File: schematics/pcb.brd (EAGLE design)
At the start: 86.4 x 110.2 mm, 39 parts, among them IC1 7805TV, IC2 4050D, IC3 LP298XS, Q1 16Mhz, Q2 16Mhz, X1 MICROSD

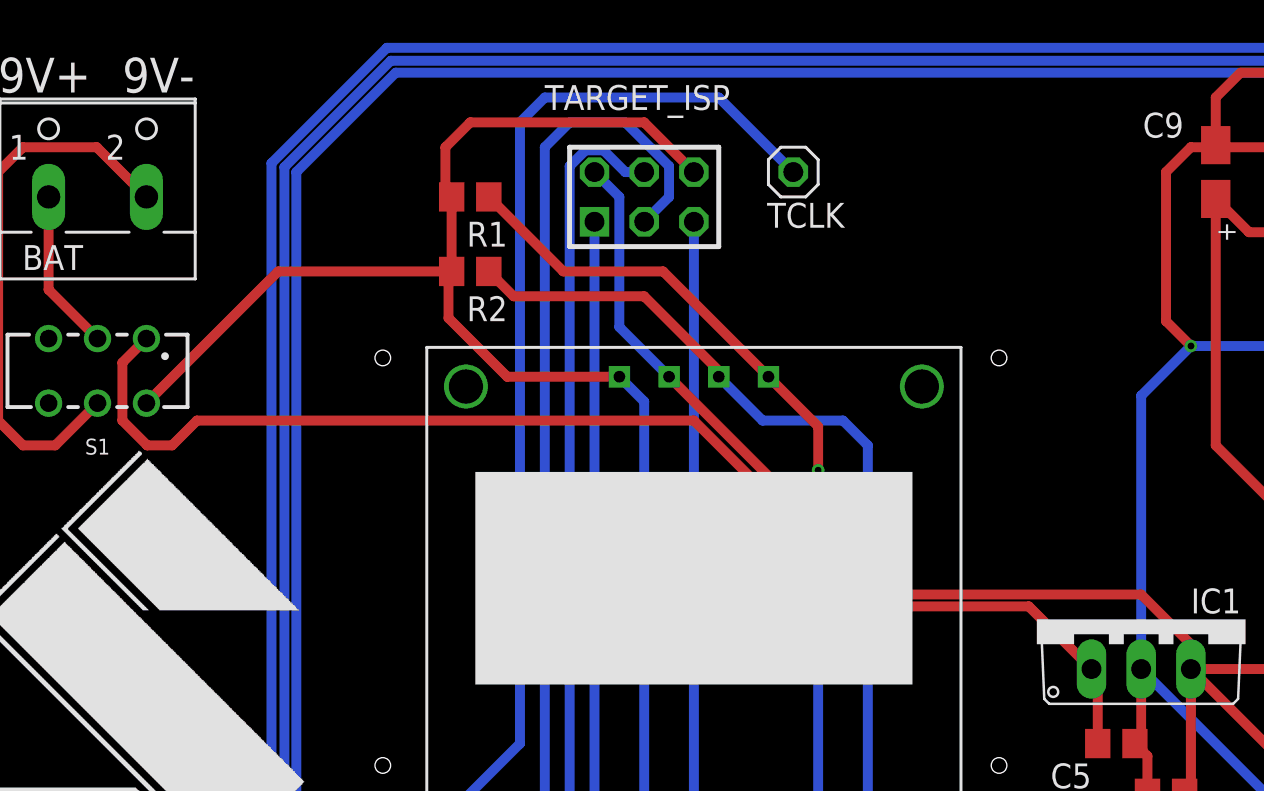
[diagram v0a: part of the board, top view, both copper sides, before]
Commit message: Fixed I2C Pull-ups being Pull-downs
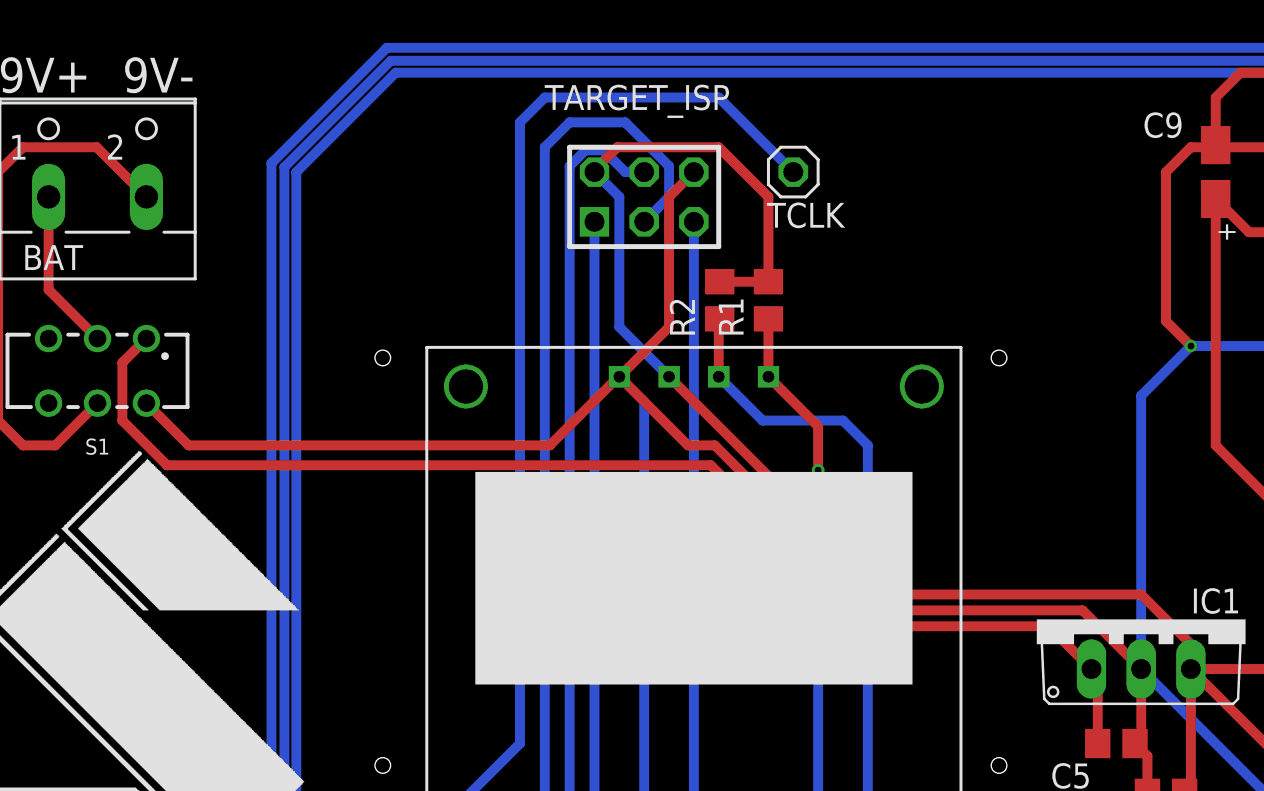
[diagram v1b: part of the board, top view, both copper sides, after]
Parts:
- moved R1 16.1 mm to (43.2, 94.3), turned to 90 degrees
- moved R2 12.8 mm to (40.7, 94.3), turned to 90 degrees
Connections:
- net +5V: now also R1.2, R2.2
- net GND: no longer R1.2, R2.2
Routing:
- net GND: track 450.5 -> 470.4 mm
- net +5V: track 276.4 -> 293.8 mm
- net N$2: track 86.9 -> 71.7 mm
- net N$1: track 87.4 -> 76.7 mm
- net 9V+: track 64.5 -> 63.4 mm
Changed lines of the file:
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@@
 <attribute name="VALUE" x="8.763" y="39.878" size="1.27" layer="27" ratio="10" rot="R270"/>
 </element>
-<element name="R1" library="rcl" library_urn="urn:adsk.eagle:library:334" package="R0805" package3d_urn="urn:adsk.eagle:package:23553/2" value="10k" x="27.94" y="99.568" smashed="yes" rot="R180">
-<attribute name="NAME" x="29.845" y="98.298" size="1.27" layer="25" rot="R180"/>
-<attribute name="POPULARITY" value="86" x="-45.72" y="168.148" size="1.778" layer="27" rot="R180" display="off"/>
-<attribute name="SPICEPREFIX" value="R" x="-45.72" y="168.148" size="1.778" layer="27" rot="R180" display="off"/>
-</element>
-<element name="R2" library="rcl" library_urn="urn:adsk.eagle:library:334" package="R0805" package3d_urn="urn:adsk.eagle:package:23553/2" value="10k" x="27.94" y="95.758" smashed="yes" rot="R180">
-<attribute name="NAME" x="29.845" y="94.488" size="1.27" layer="25" rot="R180"/>
-<attribute name="POPULARITY" value="86" x="-50.8" y="164.338" size="1.778" layer="27" rot="R180" display="off"/>
-<attribute name="SPICEPREFIX" value="R" x="-50.8" y="164.338" size="1.778" layer="27" rot="R180" display="off"/>
+<element name="R1" library="rcl" library_urn="urn:adsk.eagle:library:334" package="R0805" package3d_urn="urn:adsk.eagle:package:23553/2" value="10k" x="43.18" y="94.2848" smashed="yes" rot="R90">
+<attribute name="NAME" x="41.91" y="92.3798" size="1.27" layer="25" rot="R90"/>
+<attribute name="POPULARITY" value="86" x="111.76" y="167.9448" size="1.778" layer="27" rot="R90" display="off"/>
+<attribute name="SPICEPREFIX" value="R" x="111.76" y="167.9448" size="1.778" layer="27" rot="R90" display="off"/>
+</element>
+<element name="R2" library="rcl" library_urn="urn:adsk.eagle:library:334" package="R0805" package3d_urn="urn:adsk.eagle:package:23553/2" value="10k" x="40.6908" y="94.2848" smashed="yes" rot="R90">
+<attribute name="NAME" x="39.4208" y="92.3798" size="1.27" layer="25" rot="R90"/>
+<attribute name="POPULARITY" value="86" x="109.2708" y="173.0248" size="1.778" layer="27" rot="R90" display="off"/>
+<attribute name="SPICEPREFIX" value="R" x="109.2708" y="173.0248" size="1.778" layer="27" rot="R90" display="off"/>
 </element>
 <element name="R3" library="rcl" library_urn="urn:adsk.eagle:library:334" package="R0805" package3d_urn="urn:adsk.eagle:package:23553/2" value="10k" x="46.99" y="43.688" smashed="yes">
@@
 <contactref element="C7" pad="2"/>
 <contactref element="C11" pad="2"/>
-<contactref element="R1" pad="2"/>
-<contactref element="R2" pad="2"/>
 <contactref element="C1" pad="1"/>
 <contactref element="C2" pad="1"/>
@@
 <contactref element="X1" pad="MT1"/>
 <contactref element="S1" pad="4"/>
-<wire x1="18.12" y1="95.758" x2="11.39" y2="89.028" width="0.508" layer="1"/>
-<wire x1="26.99" y1="95.758" x2="18.12" y2="95.758" width="0.508" layer="1"/>
-<wire x1="26.99" y1="95.758" x2="26.99" y2="99.568" width="0.508" layer="1"/>
-<wire x1="26.829684375" y1="93.377684375" x2="29.82936875" y2="90.378" width="0.508" layer="1"/>
-<wire x1="29.82936875" y1="90.378" x2="35.56" y2="90.378" width="0.508" layer="1"/>
-<wire x1="39.37" y1="100.838" x2="36.83" y2="103.378" width="0.508" layer="1"/>
-<wire x1="27.94" y1="103.378" x2="26.67" y2="102.108" width="0.508" layer="1"/>
-<wire x1="26.67" y1="102.108" x2="26.67" y2="99.888" width="0.508" layer="1"/>
-<wire x1="26.67" y1="99.888" x2="26.99" y2="99.568" width="0.508" layer="1"/>
-<wire x1="36.83" y1="103.378" x2="27.94" y2="103.378" width="0.508" layer="1"/>
-<wire x1="26.99" y1="95.758" x2="26.829684375" y2="95.597684375" width="0.508" layer="1"/>
-<wire x1="26.829684375" y1="95.597684375" x2="26.829684375" y2="93.377684375" width="0.508" layer="1"/>
+<wire x1="35.51896875" y1="90.378" x2="35.56" y2="90.378" width="0.508" layer="1"/>
 <wire x1="37.15" y1="58.928" x2="36.83" y2="58.608" width="0.508" layer="1"/>
 <wire x1="36.83" y1="58.608" x2="36.83" y2="55.118" width="0.508" layer="1"/>
@@
 <wire x1="61.91" y1="71.628" x2="62.55" y2="70.988" width="0.508" layer="1"/>
 <wire x1="61.91" y1="71.628" x2="62.23" y2="71.948" width="0.508" layer="1"/>
+<wire x1="11.39" y1="89.028" x2="13.55" y2="86.868" width="0.508" layer="1"/>
+<wire x1="32.00896875" y1="86.868" x2="35.51896875" y2="90.378" width="0.508" layer="1"/>
+<wire x1="13.55" y1="86.868" x2="32.00896875" y2="86.868" width="0.508" layer="1"/>
+<wire x1="35.56" y1="90.378" x2="38.1" y2="92.918" width="0.508" layer="1"/>
+<wire x1="38.1" y1="99.568" x2="39.37" y2="100.838" width="0.508" layer="1"/>
+<wire x1="38.1" y1="92.918" x2="38.1" y2="99.568" width="0.508" layer="1"/>
+<wire x1="35.56" y1="90.378" x2="39.07" y2="86.868" width="0.508" layer="1"/>
+<wire x1="59.2328" y1="78.4352" x2="62.23" y2="75.438" width="0.508" layer="1"/>
+<wire x1="39.07" y1="86.868" x2="40.4368" y2="86.868" width="0.508" layer="1"/>
+<wire x1="40.4368" y1="86.868" x2="48.8696" y2="78.4352" width="0.508" layer="1"/>
+<wire x1="48.8696" y1="78.4352" x2="59.2328" y2="78.4352" width="0.508" layer="1"/>
 </signal>
 <signal name="+5V" class="1">
@@
 <wire x1="77.5" y1="74.138" x2="79.06" y2="74.138" width="0.508" layer="1"/>
 <wire x1="76.2" y1="75.438" x2="77.5" y2="74.138" width="0.508" layer="1"/>
+<contactref element="R1" pad="2"/>
+<contactref element="R2" pad="2"/>
+<wire x1="40.6908" y1="95.2348" x2="43.18" y2="95.2348" width="0.508" layer="1"/>
+<wire x1="43.18" y1="95.2348" x2="43.18" y2="99.568" width="0.508" layer="1"/>
+<wire x1="43.18" y1="99.568" x2="40.64" y2="102.108" width="0.508" layer="1"/>
+<wire x1="40.64" y1="102.108" x2="35.4584" y2="102.108" width="0.508" layer="1"/>
+<wire x1="35.4584" y1="102.108" x2="34.29" y2="100.9396" width="0.508" layer="1"/>
+<wire x1="34.29" y1="100.9396" x2="34.29" y2="100.838" width="0.508" layer="1"/>
 </signal>
 <signal name="N$1">
@@
 <contactref element="R2" pad="1"/>
 <contactref element="U$1" pad="SCL"/>
-<wire x1="36.83" y1="94.488" x2="40.64" y2="90.678" width="0.508" layer="1"/>
 <wire x1="40.64" y1="90.378" x2="42.88" y2="88.138" width="0.508" layer="16"/>
 <wire x1="46.99" y1="88.138" x2="48.26" y2="86.868" width="0.508" layer="16"/>
@@
 <wire x1="52.07" y1="38.608" x2="52.07" y2="44.958" width="0.508" layer="16"/>
 <wire x1="52.07" y1="44.958" x2="54.61" y2="47.498" width="0.508" layer="16"/>
-<wire x1="40.64" y1="90.378" x2="40.64" y2="90.678" width="0.508" layer="1"/>
-<wire x1="28.89" y1="95.758" x2="30.16" y2="94.488" width="0.508" layer="1"/>
-<wire x1="30.16" y1="94.488" x2="36.83" y2="94.488" width="0.508" layer="1"/>
+<wire x1="40.64" y1="90.378" x2="40.64" y2="90.7796" width="0.508" layer="1"/>
+<wire x1="40.64" y1="90.378" x2="40.64" y2="93.284" width="0.508" layer="1"/>
+<wire x1="40.64" y1="93.284" x2="40.6908" y2="93.3348" width="0.508" layer="1"/>
 </signal>
 <signal name="N$2">
@@
 <contactref element="R1" pad="1"/>
 <contactref element="U$1" pad="SDA"/>
-<wire x1="28.89" y1="99.568" x2="32.7" y2="95.758" width="0.508" layer="1"/>
-<wire x1="32.7" y1="95.758" x2="37.8" y2="95.758" width="0.508" layer="1"/>
 <wire x1="43.18" y1="90.378" x2="45.72" y2="87.838" width="0.508" layer="1"/>
 <wire x1="45.72" y1="87.838" x2="45.72" y2="85.598" width="0.508" layer="1"/>
@@
 <wire x1="48.26" y1="32.258" x2="52.07" y2="28.448" width="0.508" layer="16"/>
 <wire x1="52.07" y1="47.498" x2="49.53" y2="44.958" width="0.508" layer="16"/>
-<wire x1="37.8" y1="95.758" x2="43.18" y2="90.378" width="0.508" layer="1"/>
+<wire x1="43.18" y1="90.378" x2="43.18" y2="93.3348" width="0.508" layer="1"/>
 </signal>
 <signal name="N$3">
@@
 <contactref element="C5" pad="1"/>
 <contactref element="S1" pad="1"/>
-<wire x1="56.488" y1="78.64" x2="48.97815625" y2="78.64" width="0.508" layer="1"/>
-<wire x1="48.37015625" y1="79.248" x2="48.26" y2="79.248" width="0.508" layer="1"/>
-<wire x1="48.97815625" y1="78.64" x2="48.37015625" y2="79.248" width="0.508" layer="1"/>
-<wire x1="48.26" y1="79.248" x2="39.37" y2="88.138" width="0.508" layer="1"/>
-<wire x1="13.97" y1="88.138" x2="12.7" y2="86.868" width="0.508" layer="1"/>
-<wire x1="12.7" y1="86.868" x2="11.43" y2="86.868" width="0.508" layer="1"/>
-<wire x1="11.43" y1="86.868" x2="10.16" y2="88.138" width="0.508" layer="1"/>
+<wire x1="57.504" y1="77.624" x2="48.4616" y2="77.624" width="0.508" layer="1"/>
+<wire x1="48.4616" y1="77.624" x2="40.2336" y2="85.852" width="0.508" layer="1"/>
+<wire x1="12.446" y1="85.852" x2="10.16" y2="88.138" width="0.508" layer="1"/>
 <wire x1="10.16" y1="88.138" x2="10.16" y2="91.098" width="0.508" layer="1"/>
 <wire x1="10.16" y1="91.098" x2="11.39" y2="92.328" width="0.508" layer="1"/>
-<wire x1="59.69" y1="75.438" x2="56.488" y2="78.64" width="0.508" layer="1"/>
-<wire x1="39.37" y1="88.138" x2="13.97" y2="88.138" width="0.508" layer="1"/>
+<wire x1="59.69" y1="75.438" x2="57.504" y2="77.624" width="0.508" layer="1"/>
+<wire x1="40.2336" y1="85.852" x2="12.446" y2="85.852" width="0.508" layer="1"/>
 <wire x1="59.69" y1="75.438" x2="60.01" y2="75.118" width="0.508" layer="1"/>
 <wire x1="60.01" y1="75.118" x2="60.01" y2="71.628" width="0.508" layer="1"/>
